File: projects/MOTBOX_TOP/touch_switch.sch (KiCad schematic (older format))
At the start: 5 parts, among them J15 Conn_01x03, J16 JST_Female_3pin, J8 Conn_01x04

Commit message: Gerber files added
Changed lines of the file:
@@
 EESchema Schematic File Version 4
 LIBS:MOTBOX_TOP-cache
-LIBS:motbox_with_promini-cache
 EELAYER 26 0
 EELAYER END
 $Descr A4 11693 8268
 encoding utf-8
-Sheet 5 6
+Sheet 4 6
 Title ""
 Date ""
@@
 U 1 1 5CC06330
 P 5400 3200
-F 0 "J15" H 5480 3242 50  0000 L CNN
+F 0 "J15" H 5350 3000 50  0000 L CNN
 F 1 "Conn_01x03" H 5480 3151 50  0001 L CNN
 F 2 "Connector_Wire:SolderWirePad_1x03_P3.175mm_Drill0.8mm" H 5400 3200 50  0001 C CNN

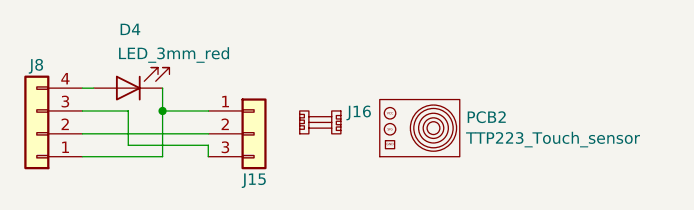
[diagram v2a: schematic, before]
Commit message: New library files and schematics with ESE31 and DT045 switches
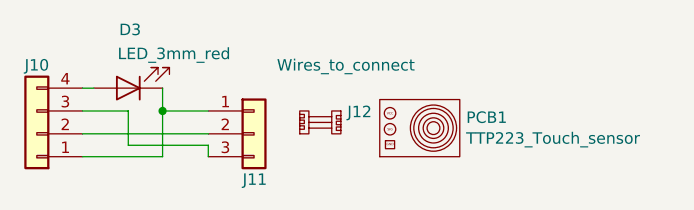
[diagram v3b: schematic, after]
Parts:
- J12: renamed from J16; value JST_Female_3pin -> Wires_to_connect
- renumbered D4 to D3, J8 to J10, J15 to J11, PCB2 to PCB1
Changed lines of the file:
@@
 EESchema Schematic File Version 4
-LIBS:MOTBOX_TOP-cache
+LIBS:MOTBOX_TOP_ESE31-cache
 EELAYER 26 0
 EELAYER END
@@
 $EndDescr
 $Comp
-L Connector_Generic:Conn_01x03 J15
+L Connector_Generic:Conn_01x03 J11
 U 1 1 5CC06330
 P 5400 3200
-F 0 "J15" H 5350 3000 50  0000 L CNN
+F 0 "J11" H 5350 3000 50  0000 L CNN
 F 1 "Conn_01x03" H 5480 3151 50  0001 L CNN
 F 2 "Connector_Wire:SolderWirePad_1x03_P3.175mm_Drill0.8mm" H 5400 3200 50  0001 C CNN
@@
 $EndComp
 $Comp
-L Device:LED D4
+L Device:LED D3
 U 1 1 5CC063D7
 P 4850 3000
-F 0 "D4" H 4842 2745 50  0000 C CNN
+F 0 "D3" H 4842 2745 50  0000 C CNN
 F 1 "LED_3mm_red" H 4650 2850 50  0000 C CNN
 F 2 "LED_THT:LED_D3.0mm" H 4850 3000 50  0001 C CNN
@@
 $EndComp
 $Comp
-L Connector_Generic:Conn_01x04 J8
+L Connector_Generic:Conn_01x04 J10
 U 1 1 5CC28BDB
 P 4450 3200
-F 0 "J8" H 4450 2900 50  0000 C CNN
+F 0 "J10" H 4450 2900 50  0000 C CNN
 F 1 "Conn_01x04" H 4370 2866 50  0001 C CNN
 F 2 "Connector_Wire:SolderWirePad_1x04_P3.175mm_Drill0.8mm" H 4450 3200 50  0001 C CNN
@@
 	5000 3000 5000 3100
 $Comp
-L hitesh_custom:TTP223_Touch_sensor PCB2
+L hitesh_custom:TTP223_Touch_sensor PCB1
 U 1 1 5CC296A0
 P 5950 3300
-F 0 "PCB2" H 6328 3471 50  0000 L CNN
+F 0 "PCB1" H 6328 3471 50  0000 L CNN
 F 1 "TTP223_Touch_sensor" H 6328 3380 50  0000 L CNN
 F 2 "" H 5950 3300 50  0001 C CNN
@@
 $EndComp
 $Comp
-L hitesh_custom:JST_Female_3pin J16
+L hitesh_custom:JST_Female_3pin J12
 U 1 1 5CC29F55
 P 5500 3200
-F 0 "J16" H 5808 3296 50  0000 L CNN
-F 1 "JST_Female_3pin" H 5808 3205 50  0001 L CNN
+F 0 "J12" H 5808 3296 50  0000 L CNN
+F 1 "Wires_to_connect" H 5500 3500 50  0000 L CNN
 F 2 "" H 5500 3200 50  0001 C CNN
 F 3 "" H 5500 3200 50  0001 C CNN
